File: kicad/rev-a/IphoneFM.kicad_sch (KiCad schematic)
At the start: 8 parts, among them U1 STM32U535CEU6, U2 LMX2571NJKR, U3 AP2112K-3.3TRG1, U4 SI4705-D60-GM, U5 PE42421SCAA-Z, U6 USBLC6-2SC6, U7 PE43711B-Z, Y2 OT322520MJBA4SL 20MHz

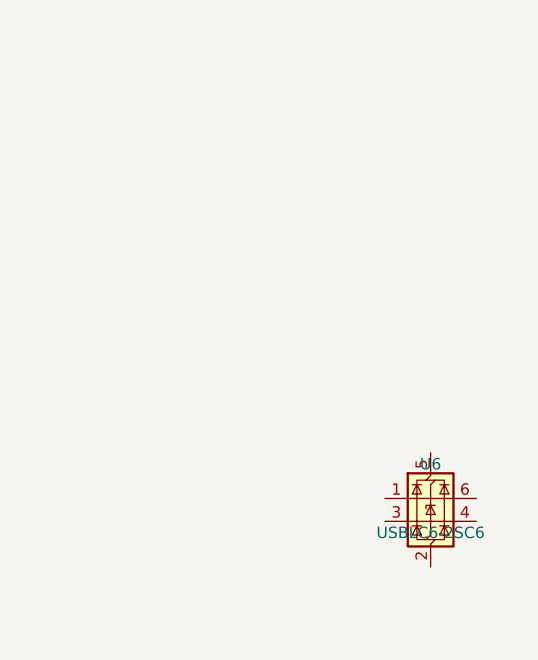
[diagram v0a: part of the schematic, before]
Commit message: Step 1.12: J1 USB-C placed (KiCad USB_C_Receptacle_USB2.0_16P)
Co-Authored-By: Claude Opus 5.5 <noreply@anthropic.com>
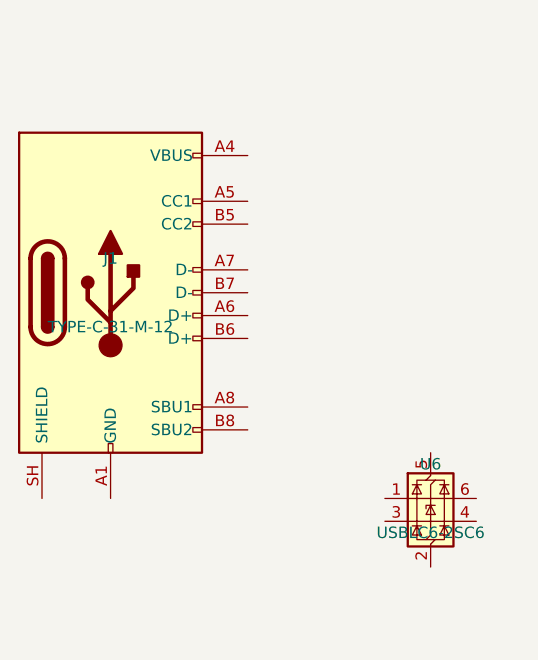
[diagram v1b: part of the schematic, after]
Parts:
- added J1: TYPE-C-31-M-12, symbol Connector:USB_C_Receptacle_USB2.0_16P
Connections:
- new net: J1.A1 (GND), J1.A12 (GND), J1.B1 (GND), J1.B12 (GND)
- new net: J1.A4 (VBUS), J1.A9 (VBUS), J1.B4 (VBUS), J1.B9 (VBUS)
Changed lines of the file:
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@@
+		)
+	)
+	(symbol
+		(lib_id "Connector:USB_C_Receptacle_USB2.0_16P")
+		(at 38.1 71.12 0)
+		(unit 1)
+		(exclude_from_sim no)
+		(in_bom yes)
+		(on_board yes)
+		(dnp no)
+		(property "Reference" "J1"
+			(at 38.1 67.31 0)
+			(effects (font (size 1.27 1.27)))
+		)
+		(property "Value" "TYPE-C-31-M-12"
+			(at 38.1 74.93 0)
+			(effects (font (size 1.27 1.27)))
+		)
+		(property "Footprint" ""
+			(at 38.1 71.12 0)
+			(effects (font (size 1.27 1.27)) (hide yes))
+		)
+		(property "Datasheet" "~"
+			(at 38.1 71.12 0)
+			(effects (font (size 1.27 1.27)) (hide yes))
+		)
+		(instances
+			(project "IphoneFM"
+				(path "/efee88c9-028d-4fdb-86e0-0a4145b330e1"
+					(reference "J1") (unit 1)
+				)
+			)
 		)
 	)

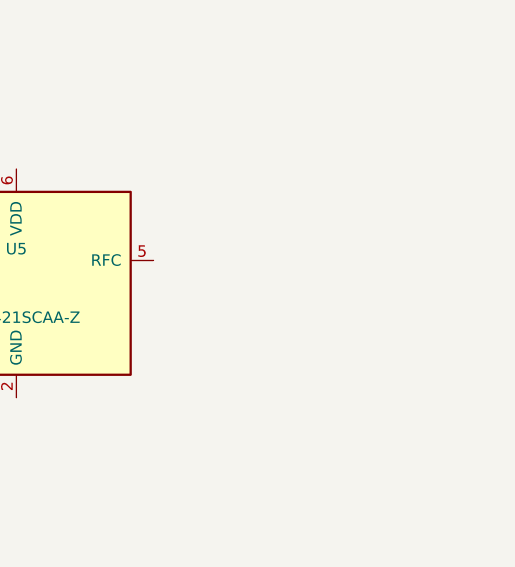
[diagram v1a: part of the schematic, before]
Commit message: Step 1.13: J2 SMA placed (KiCad Conn_Coaxial); netlist.json J2 follows the 2-pin coaxial convention
Co-Authored-By: Claude Opus 5.5 <noreply@anthropic.com>
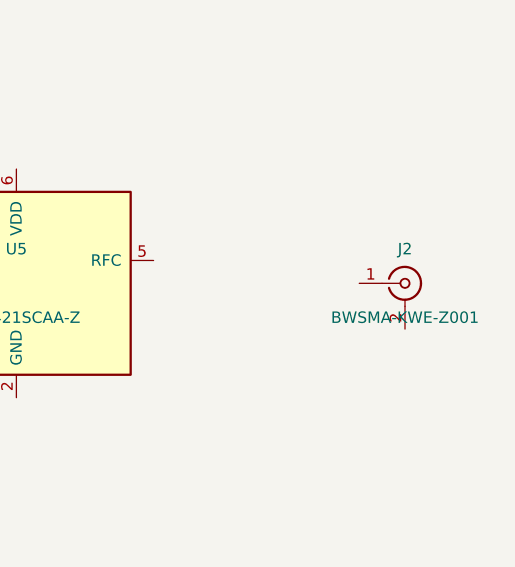
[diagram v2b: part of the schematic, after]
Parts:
- added J2: BWSMA-KWE-Z001, symbol Connector:Conn_Coaxial
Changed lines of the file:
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@@
+		)
+	)
+	(symbol
+		(lib_id "Connector:Conn_Coaxial")
+		(at 563.88 152.4 0)
+		(unit 1)
+		(exclude_from_sim no)
+		(in_bom yes)
+		(on_board yes)
+		(dnp no)
+		(property "Reference" "J2"
+			(at 563.88 148.59 0)
+			(effects (font (size 1.27 1.27)))
+		)
+		(property "Value" "BWSMA-KWE-Z001"
+			(at 563.88 156.21 0)
+			(effects (font (size 1.27 1.27)))
+		)
+		(property "Footprint" ""
+			(at 563.88 152.4 0)
+			(effects (font (size 1.27 1.27)) (hide yes))
+		)
+		(property "Datasheet" "~"
+			(at 563.88 152.4 0)
+			(effects (font (size 1.27 1.27)) (hide yes))
+		)
+		(instances
+			(project "IphoneFM"
+				(path "/efee88c9-028d-4fdb-86e0-0a4145b330e1"
+					(reference "J2") (unit 1)
+				)
+			)
 		)
 	)

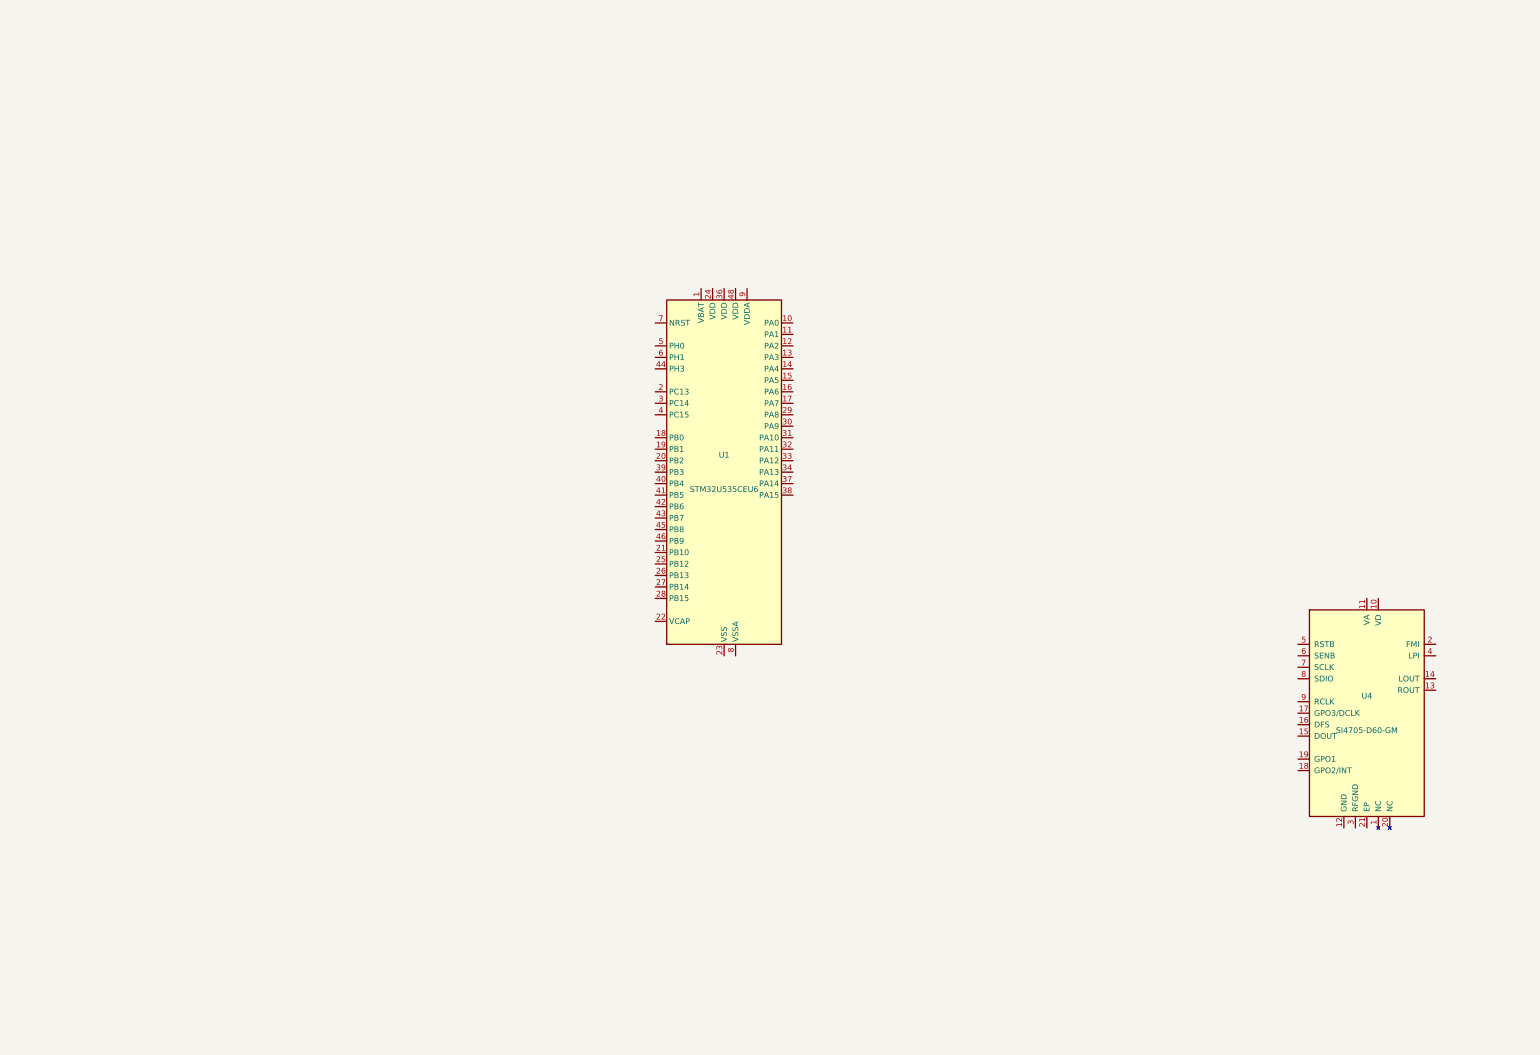
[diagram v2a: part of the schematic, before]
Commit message: Step 1.14: SW1 (project MSK12C02 symbol), SW2 (SW_Push), SW3 (SW_DIP_x06) placed
Co-Authored-By: Claude Opus 5.5 <noreply@anthropic.com>
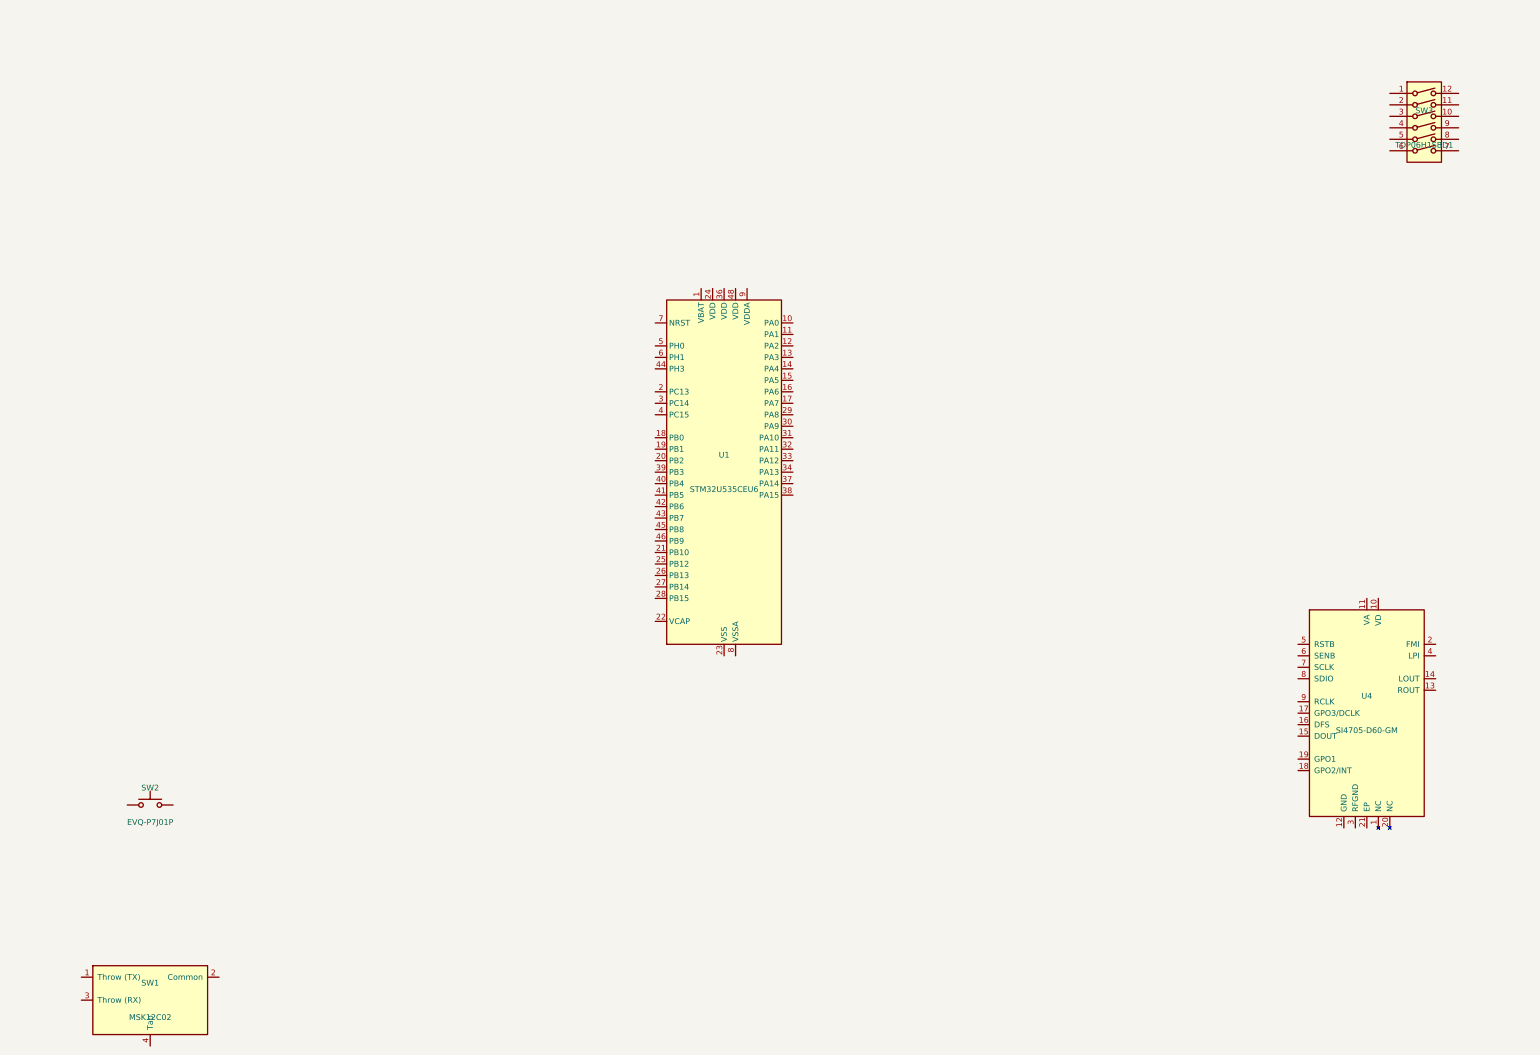
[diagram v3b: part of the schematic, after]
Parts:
- added SW1: MSK12C02, symbol IphoneFM:MSK12C02
- added SW2: EVQ-P7J01P, symbol Switch:SW_Push
- added SW3: TDP06H1SBD1, symbol Switch:SW_DIP_x06
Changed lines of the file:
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@@
+		)
+	)
+	(symbol
+		(lib_id "IphoneFM:MSK12C02")
+		(at 96.52 368.3 0)
+		(unit 1)
+		(exclude_from_sim no)
+		(in_bom yes)
+		(on_board yes)
+		(dnp no)
+		(property "Reference" "SW1"
+			(at 96.52 364.49 0)
+			(effects (font (size 1.27 1.27)))
+		)
+		(property "Value" "MSK12C02"
+			(at 96.52 372.11 0)
+			(effects (font (size 1.27 1.27)))
+		)
+		(property "Footprint" ""
+			(at 96.52 368.3 0)
+			(effects (font (size 1.27 1.27)) (hide yes))
+		)
+		(property "Datasheet" "~"
+			(at 96.52 368.3 0)
+			(effects (font (size 1.27 1.27)) (hide yes))
+		)
+		(instances
+			(project "IphoneFM"
+				(path "/efee88c9-028d-4fdb-86e0-0a4145b330e1"
+					(reference "SW1") (unit 1)
+				)
+			)
+		)
+	)
+	(symbol
+		(lib_id "Switch:SW_Push")
+		(at 96.52 325.12 0)
+		(unit 1)
+		(exclude_from_sim no)
+		(in_bom yes)
+		(on_board yes)
+		(dnp no)
+		(property "Reference" "SW2"
+			(at 96.52 321.31 0)
+			(effects (font (size 1.27 1.27)))
+		)
+		(property "Value" "EVQ-P7J01P"
+			(at 96.52 328.93 0)
+			(effects (font (size 1.27 1.27)))
+		)
+		(property "Footprint" ""
+			(at 96.52 325.12 0)
+			(effects (font (size 1.27 1.27)) (hide yes))
+		)
+		(property "Datasheet" "~"
+			(at 96.52 325.12 0)
+			(effects (font (size 1.27 1.27)) (hide yes))
+		)
+		(instances
+			(project "IphoneFM"
+				(path "/efee88c9-028d-4fdb-86e0-0a4145b330e1"
+					(reference "SW2") (unit 1)
+				)
+			)
+		)
+	)
+	(symbol
+		(lib_id "Switch:SW_DIP_x06")
+		(at 378.46 175.26 0)
+		(unit 1)
+		(exclude_from_sim no)
+		(in_bom yes)
+		(on_board yes)
+		(dnp no)
+		(property "Reference" "SW3"
+			(at 378.46 171.45 0)
+			(effects (font (size 1.27 1.27)))
+		)
+		(property "Value" "TDP06H1SBD1"
+			(at 378.46 179.07 0)
+			(effects (font (size 1.27 1.27)))
+		)
+		(property "Footprint" ""
+			(at 378.46 175.26 0)
+			(effects (font (size 1.27 1.27)) (hide yes))
+		)
+		(property "Datasheet" "~"
+			(at 378.46 175.26 0)
+			(effects (font (size 1.27 1.27)) (hide yes))
+		)
+		(instances
+			(project "IphoneFM"
+				(path "/efee88c9-028d-4fdb-86e0-0a4145b330e1"
+					(reference "SW3") (unit 1)
+				)
+			)
 		)
 	)

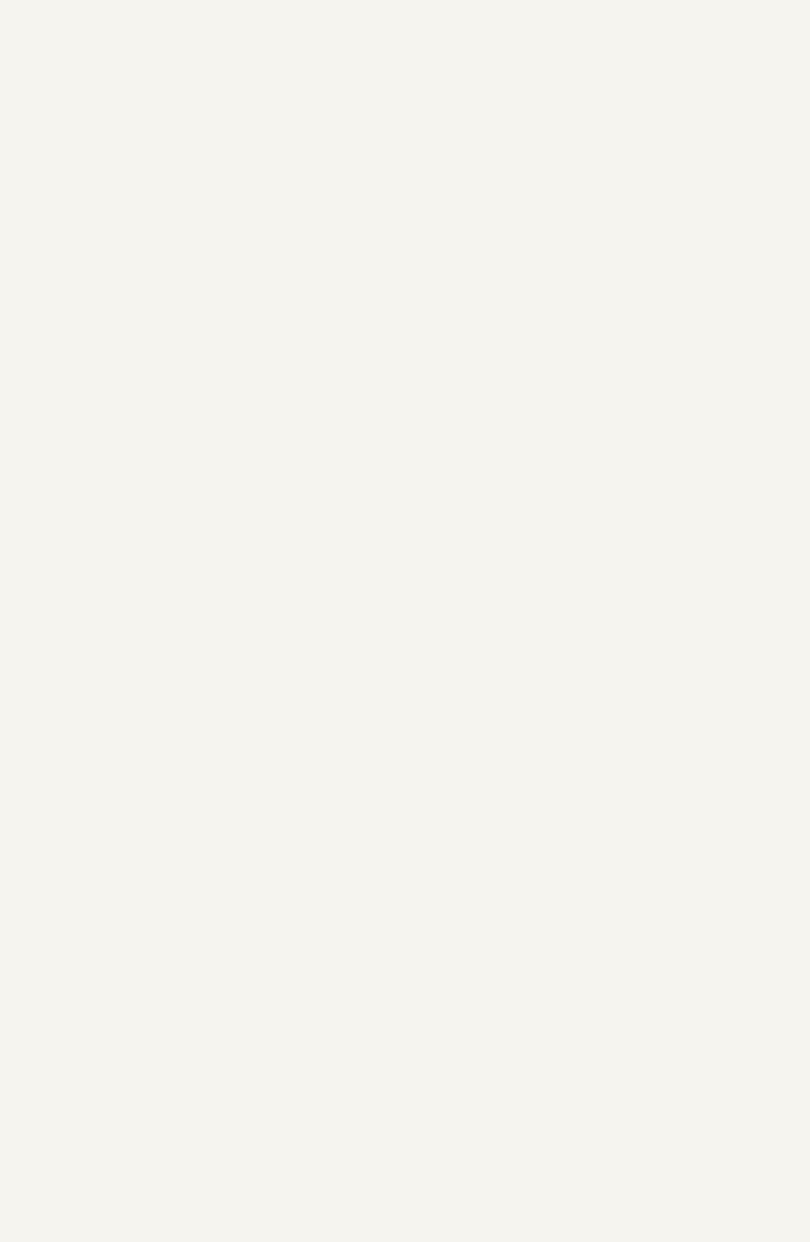
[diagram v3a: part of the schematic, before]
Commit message: Step 1.15: RV1-RV3 placed from a project RK10J11R0A0H symbol (7 pins incl. dummy and mounting lands)
Co-Authored-By: Claude Opus 5.5 <noreply@anthropic.com>
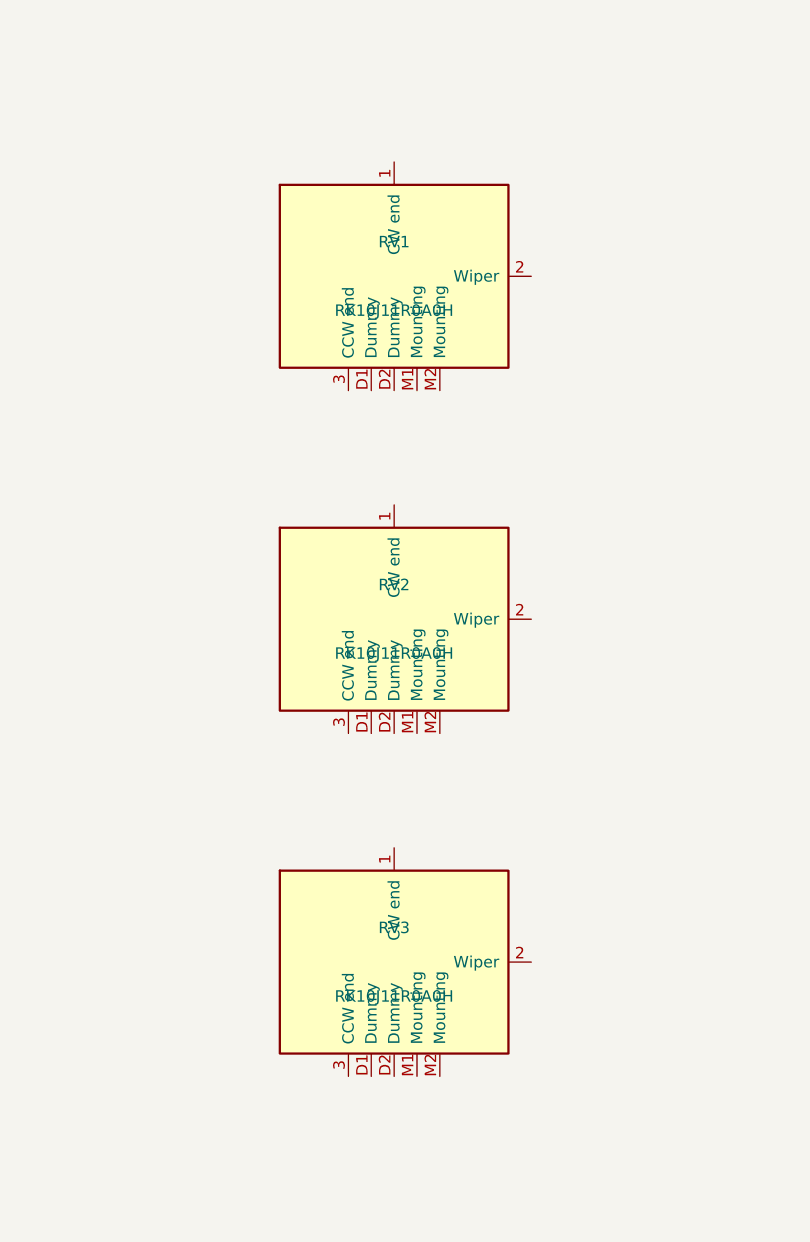
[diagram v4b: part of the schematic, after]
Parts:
- added RV1, RV2, RV3: RK10J11R0A0H, symbol IphoneFM:RK10J11R0A0H
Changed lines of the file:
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@@
+		)
+	)
+	(symbol
+		(lib_id "IphoneFM:RK10J11R0A0H")
+		(at 96.52 198.12 0)
+		(unit 1)
+		(exclude_from_sim no)
+		(in_bom yes)
+		(on_board yes)
+		(dnp no)
+		(property "Reference" "RV1"
+			(at 96.52 194.31 0)
+			(effects (font (size 1.27 1.27)))
+		)
+		(property "Value" "RK10J11R0A0H"
+			(at 96.52 201.93 0)
+			(effects (font (size 1.27 1.27)))
+		)
+		(property "Footprint" ""
+			(at 96.52 198.12 0)
+			(effects (font (size 1.27 1.27)) (hide yes))
+		)
+		(property "Datasheet" "~"
+			(at 96.52 198.12 0)
+			(effects (font (size 1.27 1.27)) (hide yes))
+		)
+		(instances
+			(project "IphoneFM"
+				(path "/efee88c9-028d-4fdb-86e0-0a4145b330e1"
+					(reference "RV1") (unit 1)
+				)
+			)
+		)
+	)
+	(symbol
+		(lib_id "IphoneFM:RK10J11R0A0H")
+		(at 96.52 236.22 0)
+		(unit 1)
+		(exclude_from_sim no)
+		(in_bom yes)
+		(on_board yes)
+		(dnp no)
+		(property "Reference" "RV2"
+			(at 96.52 232.41 0)
+			(effects (font (size 1.27 1.27)))
+		)
+		(property "Value" "RK10J11R0A0H"
+			(at 96.52 240.03 0)
+			(effects (font (size 1.27 1.27)))
+		)
+		(property "Footprint" ""
+			(at 96.52 236.22 0)
+			(effects (font (size 1.27 1.27)) (hide yes))
+		)
+		(property "Datasheet" "~"
+			(at 96.52 236.22 0)
+			(effects (font (size 1.27 1.27)) (hide yes))
+		)
+		(instances
+			(project "IphoneFM"
+				(path "/efee88c9-028d-4fdb-86e0-0a4145b330e1"
+					(reference "RV2") (unit 1)
+				)
+			)
+		)
+	)
+	(symbol
+		(lib_id "IphoneFM:RK10J11R0A0H")
+		(at 96.52 274.32 0)
+		(unit 1)
+		(exclude_from_sim no)
+		(in_bom yes)
+		(on_board yes)
+		(dnp no)
+		(property "Reference" "RV3"
+			(at 96.52 270.51 0)
+			(effects (font (size 1.27 1.27)))
+		)
+		(property "Value" "RK10J11R0A0H"
+			(at 96.52 278.13 0)
+			(effects (font (size 1.27 1.27)))
+		)
+		(property "Footprint" ""
+			(at 96.52 274.32 0)
+			(effects (font (size 1.27 1.27)) (hide yes))
+		)
+		(property "Datasheet" "~"
+			(at 96.52 274.32 0)
+			(effects (font (size 1.27 1.27)) (hide yes))
+		)
+		(instances
+			(project "IphoneFM"
+				(path "/efee88c9-028d-4fdb-86e0-0a4145b330e1"
+					(reference "RV3") (unit 1)
+				)
+			)
 		)
 	)
